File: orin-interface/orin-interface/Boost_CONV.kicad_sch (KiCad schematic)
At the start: 21 parts, among them Q1 BSC094N06LS5ATMA1, U7 LT8357EMSE-PBF, U8 FSV10100V

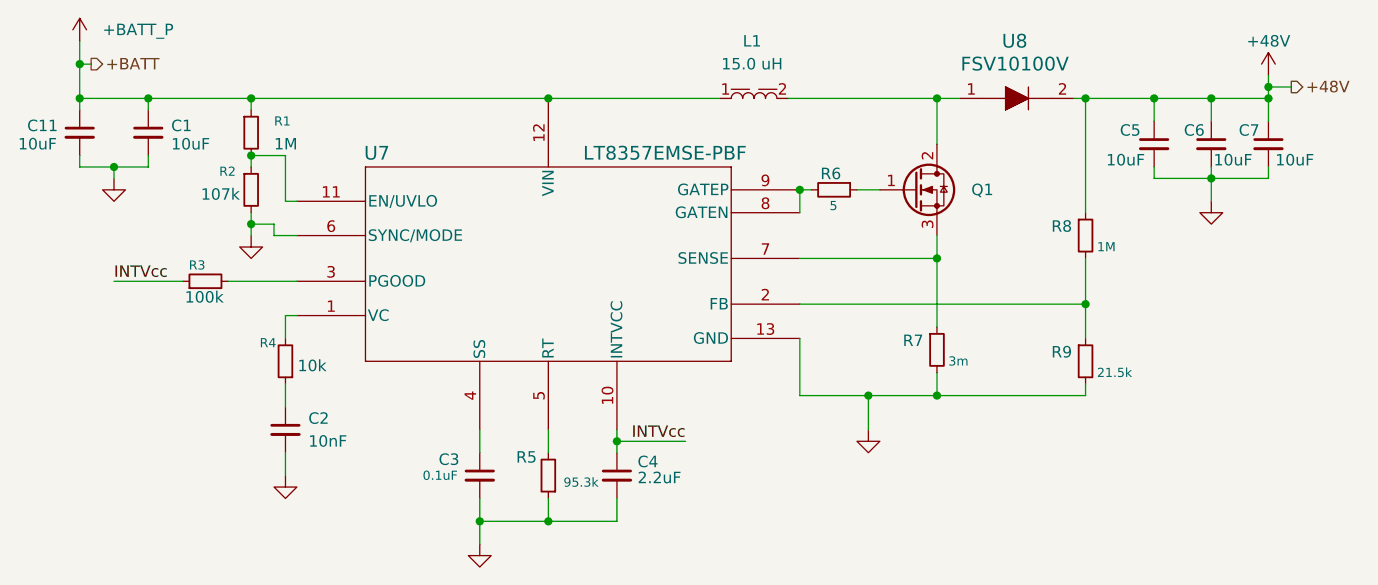
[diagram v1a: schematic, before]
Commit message: orin-interface: PoE channels, buses, 3V3 regulator, ERC fixes
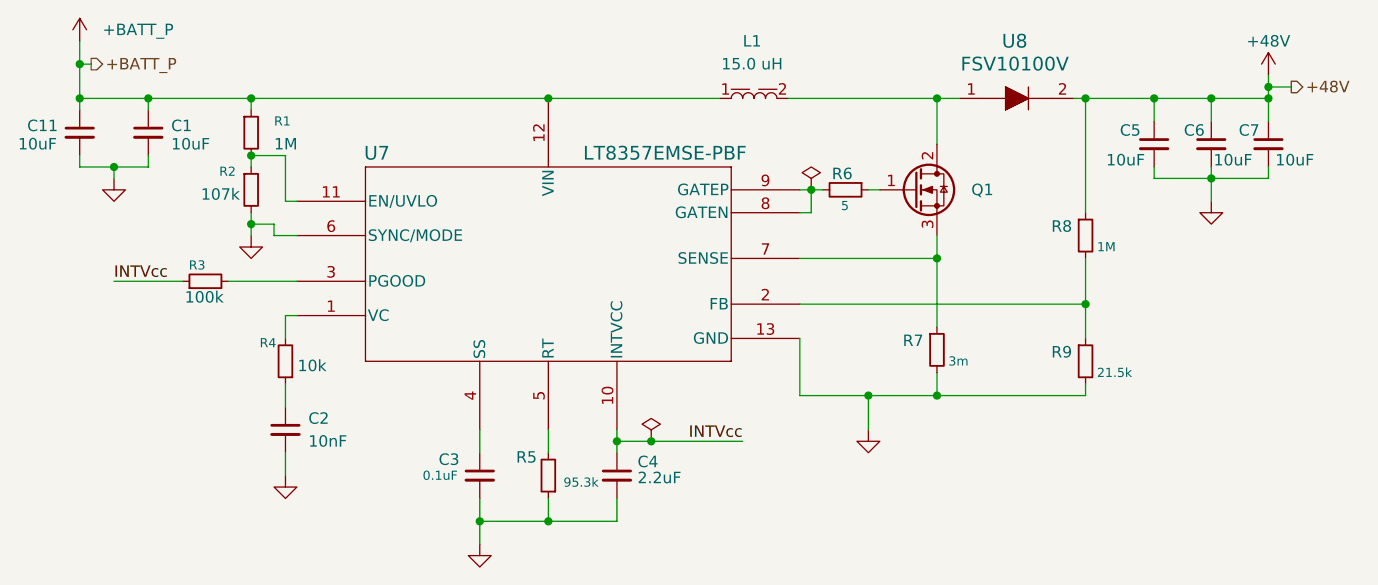
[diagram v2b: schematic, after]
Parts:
- C1, C11, C2, C3, C4, C5, C6, C7: footprint (none) -> Capacitor_SMD:C_0603_1608Metric_Pad1.08x0.95mm_HandSolder
- R1, R2, R3, R4, R5, R6, R7, R8, R9: footprint (none) -> Resistor_SMD:R_0603_1608Metric_Pad0.98x0.95mm_HandSolder
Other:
- moved on the sheet: R6
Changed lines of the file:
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@@
 	(paper "A5")
 	(junction
+		(at 100.33 81.28)
+		(diameter 0)
+		(color 0 0 0 0)
+	)
+	(junction
 		(at 36.83 39.37)
 		(diameter 0)
@@
 	)
 	(junction
+		(at 118.11 53.34)
+		(diameter 0)
+		(color 0 0 0 0)
+	)
+	(junction
 		(at 148.59 66.04)
 		(diameter 0)
@@
 		(color 0 0 0 0)
 	)
-	(junction
-		(at 116.84 53.34)
-		(diameter 0)
-		(color 0 0 0 0)
-	)
 	(wire
 		(pts
@@
 	(wire
 		(pts
+			(xy 118.11 55.88) (xy 116.84 55.88)
+		)
+		(stroke
+			(width 0)
+			(type default)
+		)
+	)
+	(wire
+		(pts
 			(xy 55.88 43.18) (xy 88.9 43.18)
 		)
@@
 	(wire
 		(pts
+			(xy 100.33 81.28) (xy 110.49 81.28)
+		)
+		(stroke
+			(width 0)
+			(type default)
+		)
+	)
+	(wire
+		(pts
 			(xy 168.91 45.72) (xy 168.91 43.18)
 		)
@@
 	(wire
 		(pts
+			(xy 118.11 53.34) (xy 119.38 53.34)
+		)
+		(stroke
+			(width 0)
+			(type default)
+		)
+	)
+	(wire
+		(pts
 			(xy 162.56 52.07) (xy 162.56 54.61)
 		)
@@
 	(wire
 		(pts
-			(xy 96.52 81.28) (xy 104.14 81.28)
+			(xy 96.52 81.28) (xy 100.33 81.28)
 		)
 		(stroke
@@
 	(wire
 		(pts
-			(xy 123.19 53.34) (xy 125.73 53.34)
+			(xy 124.46 53.34) (xy 125.73 53.34)
 		)
 		(stroke
@@
 	(wire
 		(pts
-			(xy 116.84 53.34) (xy 116.84 55.88)
+			(xy 118.11 53.34) (xy 118.11 55.88)
 		)
 		(stroke
@@
 	)
 	(label "INTVcc"
-		(at 104.14 81.28 180)
+		(at 110.49 81.28 180)
 		(effects
 			(font
@@
 		)
 	)
-	(hierarchical_label "+BATT"
+	(hierarchical_label "+BATT_P"
 		(shape output)
 		(at 38.1 39.37 0)
@@
 			)
 		)
-		(property "Footprint" ""
+		(property "Footprint" "Capacitor_SMD:C_0603_1608Metric_Pad1.08x0.95mm_HandSolder"
 			(at 156.21 48.26 0)
 			(hide yes)
@@
 			)
 		)
-		(property "Footprint" ""
+		(property "Footprint" "Resistor_SMD:R_0603_1608Metric_Pad0.98x0.95mm_HandSolder"
 			(at 88.9 85.09 0)
 			(hide yes)
@@
 			)
 		)
-		(property "Footprint" ""
+		(property "Footprint" "Capacitor_SMD:C_0603_1608Metric_Pad1.08x0.95mm_HandSolder"
 			(at 36.83 46.99 0)
 			(hide yes)
@@
 			)
 		)
-		(property "Footprint" ""
+		(property "Footprint" "Resistor_SMD:R_0603_1608Metric_Pad0.98x0.95mm_HandSolder"
 			(at 50.8 63.5 0)
 			(hide yes)
@@
 			)
 		)
-		(property "Footprint" ""
+		(property "Footprint" "Capacitor_SMD:C_0603_1608Metric_Pad1.08x0.95mm_HandSolder"
 			(at 162.56 48.26 0)
 			(hide yes)
@@
 			)
 		)
-		(property "Footprint" ""
+		(property "Footprint" "Resistor_SMD:R_0603_1608Metric_Pad0.98x0.95mm_HandSolder"
 			(at 55.88 46.99 0)
 			(hide yes)
@@
 			)
 		)
-		(property "Footprint" ""
+		(property "Footprint" "Capacitor_SMD:C_0603_1608Metric_Pad1.08x0.95mm_HandSolder"
 			(at 96.52 85.09 0)
 			(hide yes)
@@
 	)
 	(symbol
+		(lib_id "power:PWR_FLAG")
+		(at 118.11 53.34 0)
+		(unit 1)
+		(body_style 1)
+		(exclude_from_sim no)
+		(in_bom yes)
+		(on_board yes)
+		(in_pos_files yes)
+		(dnp no)
+		(fields_autoplaced yes)
+		(property "Reference" "#FLG03"
+			(at 118.11 51.435 0)
+			(hide yes)
+			(show_name no)
+			(do_not_autoplace no)
+			(effects
+				(font
+					(size 1.27 1.27)
+				)
+			)
+		)
+		(property "Value" "PWR_FLAG"
+			(at 118.11 48.26 0)
+			(hide yes)
+			(show_name no)
+			(do_not_autoplace no)
+			(effects
+				(font
+					(size 1.27 1.27)
+				)
+			)
+		)
+		(property "Footprint" ""
+			(at 118.11 53.34 0)
+			(hide yes)
+			(show_name no)
+			(do_not_autoplace no)
+			(effects
+				(font
+					(size 1.27 1.27)
+				)
+			)
+		)
+		(property "Datasheet" ""
+			(at 118.11 53.34 0)
+			(hide yes)
+			(show_name no)
+			(do_not_autoplace no)
+			(effects
+				(font
+					(size 1.27 1.27)
+				)
+			)
+		)
+		(property "Description" "Special symbol for telling ERC where power comes from"
+			(at 118.11 53.34 0)
+			(hide yes)
+			(show_name no)
+			(do_not_autoplace no)
+			(effects
+				(font
+					(size 1.27 1.27)
+				)
+			)
+		)
+		(pin "1"
+		)
+		(instances
+			(project "orin-interface"
+				(path "/18aef7c7-2f0e-4a2c-9e5d-7b655e80b6a3/854e6725-7577-4f39-ac5c-b29c5dbf90aa"
+					(reference "#FLG03")
+					(unit 1)
+				)
+			)
+		)
+	)
+	(symbol
 		(lib_id "power:GND")
 		(at 40.64 52.07 0)
@@
 			)
 		)
-		(property "Footprint" ""
+		(property "Footprint" "Capacitor_SMD:C_0603_1608Metric_Pad1.08x0.95mm_HandSolder"
 			(at 44.45 46.99 0)
 			(hide yes)
@@
 			)
 		)
-		(property "Footprint" ""
+		(property "Footprint" "Resistor_SMD:R_0603_1608Metric_Pad0.98x0.95mm_HandSolder"
 			(at 55.88 53.34 0)
 			(hide yes)
@@
 			)
 		)
-		(property "Footprint" ""
+		(property "Footprint" "Resistor_SMD:R_0603_1608Metric_Pad0.98x0.95mm_HandSolder"
 			(at 148.59 58.42 0)
 			(hide yes)
@@
 			)
 		)
-		(property "Footprint" ""
+		(property "Footprint" "Resistor_SMD:R_0603_1608Metric_Pad0.98x0.95mm_HandSolder"
 			(at 132.08 71.12 0)
 			(hide yes)
@@
 			)
 		)
-		(property "Footprint" ""
+		(property "Footprint" "Capacitor_SMD:C_0603_1608Metric_Pad1.08x0.95mm_HandSolder"
 			(at 59.69 80.01 0)
 			(hide yes)
@@
 			)
 		)
-		(property "Footprint" ""
+		(property "Footprint" "Capacitor_SMD:C_0603_1608Metric_Pad1.08x0.95mm_HandSolder"
 			(at 168.91 48.26 0)
 			(hide yes)
@@
 	(symbol
 		(lib_id "Device:R_Small")
-		(at 120.65 53.34 270)
+		(at 121.92 53.34 270)
 		(unit 1)
 		(body_style 1)
@@
 		(dnp no)
 		(property "Reference" "R6"
-			(at 119.126 51.562 90)
+			(at 120.396 51.562 90)
 			(show_name no)
 			(do_not_autoplace no)
@@
 		)
 		(property "Value" "5"
-			(at 120.142 55.118 90)
+			(at 121.412 55.118 90)
 			(show_name no)
 			(do_not_autoplace no)
@@
 			)
 		)
-		(property "Footprint" ""
-			(at 120.65 53.34 0)
+		(property "Footprint" "Resistor_SMD:R_0603_1608Metric_Pad0.98x0.95mm_HandSolder"
+			(at 121.92 53.34 0)
 			(hide yes)
 			(show_name no)
@@
 		)
 		(property "Datasheet" ""
-			(at 120.65 53.34 0)
+			(at 121.92 53.34 0)
 			(hide yes)
 			(show_name no)
@@
 		)
 		(property "Description" "Resistor, small symbol"
-			(at 120.65 53.34 0)
+			(at 121.92 53.34 0)
 			(hide yes)
 			(show_name no)
@@
 			)
 		)
-		(property "Footprint" ""
+		(property "Footprint" "Capacitor_SMD:C_0603_1608Metric_Pad1.08x0.95mm_HandSolder"
 			(at 81.28 85.09 0)
 			(hide yes)
@@
 			)
 		)
-		(property "Footprint" ""
+		(property "Footprint" "Resistor_SMD:R_0603_1608Metric_Pad0.98x0.95mm_HandSolder"
 			(at 148.59 72.39 0)
 			(hide yes)
@@
 	)
 	(symbol
+		(lib_id "power:PWR_FLAG")
+		(at 100.33 81.28 0)
+		(unit 1)
+		(body_style 1)
+		(exclude_from_sim no)
+		(in_bom yes)
+		(on_board yes)
+		(in_pos_files yes)
+		(dnp no)
+		(fields_autoplaced yes)
+		(property "Reference" "#FLG04"
+			(at 100.33 79.375 0)
+			(hide yes)
+			(show_name no)
+			(do_not_autoplace no)
+			(effects
+				(font
+					(size 1.27 1.27)
+				)
+			)
+		)
+		(property "Value" "PWR_FLAG"
+			(at 100.33 76.2 0)
+			(hide yes)
+			(show_name no)
+			(do_not_autoplace no)
+			(effects
+				(font
+					(size 1.27 1.27)
+				)
+			)
+		)
+		(property "Footprint" ""
+			(at 100.33 81.28 0)
+			(hide yes)
+			(show_name no)
+			(do_not_autoplace no)
+			(effects
+				(font
+					(size 1.27 1.27)
+				)
+			)
+		)
+		(property "Datasheet" ""
+			(at 100.33 81.28 0)
+			(hide yes)
+			(show_name no)
+			(do_not_autoplace no)
+			(effects
+				(font
+					(size 1.27 1.27)
+				)
+			)
+		)
+		(property "Description" "Special symbol for telling ERC where power comes from"
+			(at 100.33 81.28 0)
+			(hide yes)
+			(show_name no)
+			(do_not_autoplace no)
+			(effects
+				(font
+					(size 1.27 1.27)
+				)
+			)
+		)
+		(pin "1"
+		)
+		(instances
+			(project "orin-interface"
+				(path "/18aef7c7-2f0e-4a2c-9e5d-7b655e80b6a3/854e6725-7577-4f39-ac5c-b29c5dbf90aa"
+					(reference "#FLG04")
+					(unit 1)
+				)
+			)
+		)
+	)
+	(symbol
 		(lib_id "Device:R_Small")
 		(at 59.69 72.39 180)
@@
 			)
 		)
-		(property "Footprint" ""
+		(property "Footprint" "Resistor_SMD:R_0603_1608Metric_Pad0.98x0.95mm_HandSolder"
 			(at 59.69 72.39 0)
 			(hide yes)

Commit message: orin-interface: add ETH connector sheets and Mate-connectors footprint lib; update orin-bob
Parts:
- removed L1: 15.0 uH, Inductor_SMD_Wurth:L_Wurth_WE-XHMI-1010P, symbol 744393605150:1010P_744393605150
- added L2: 15.0 uH, WE-PD:L_Wurth_WE-PD-1260P, symbol WE-PD:1260P_7447706150
- R7: value 3m -> 10m
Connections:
- net +48V: now also U8.3; no longer U8.2
- net +BATT_P: now also L2.1
- net at Q1.3, R7.1, U7.7 (SENSE): now also Q1.1, Q1.2
- net at R6.1: now also Q1.4; no longer Q1.1
- net at U8.1: now also Q1.5, Q1.6, Q1.7, Q1.8, Q1.9, U8.2, L2.2; no longer Q1.2
